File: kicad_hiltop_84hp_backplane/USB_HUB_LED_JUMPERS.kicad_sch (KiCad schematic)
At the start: 59 parts, among them U5 USB2517, Y2 24Mhz Xtal

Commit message: Added io tracking on the layout
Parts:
- R68, R69, R70, R71, R72, R73, R74, R75, R76, R77, R78, R79, R80, R81: value 330 -> 330R
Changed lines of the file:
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@@
     (in_bom yes) (on_board yes)
     (property "Reference" "R72" (id 0) (at 251.46 121.285 90))
-    (property "Value" "330" (id 1) (at 255.27 122.555 90))
+    (property "Value" "330R" (id 1) (at 255.27 122.555 90))
     (property "Footprint" "Resistor_SMD:R_0402_1005Metric" (id 2) (at 255.27 120.777 90)
       (effects (font (size 1.27 1.27)) hide)
@@
     (in_bom yes) (on_board yes)
     (property "Reference" "R73" (id 0) (at 251.46 125.095 90))
-    (property "Value" "330" (id 1) (at 255.27 126.365 90))
+    (property "Value" "330R" (id 1) (at 255.27 126.365 90))
     (property "Footprint" "Resistor_SMD:R_0402_1005Metric" (id 2) (at 255.27 124.587 90)
       (effects (font (size 1.27 1.27)) hide)
@@
     (in_bom yes) (on_board yes)
     (property "Reference" "R71" (id 0) (at 251.46 109.855 90))
-    (property "Value" "330" (id 1) (at 255.27 111.125 90))
+    (property "Value" "330R" (id 1) (at 255.27 111.125 90))
     (property "Footprint" "Resistor_SMD:R_0402_1005Metric" (id 2) (at 255.27 109.347 90)
       (effects (font (size 1.27 1.27)) hide)
@@
     (in_bom yes) (on_board yes)
     (property "Reference" "R70" (id 0) (at 251.46 106.045 90))
-    (property "Value" "330" (id 1) (at 255.27 107.315 90))
+    (property "Value" "330R" (id 1) (at 255.27 107.315 90))
     (property "Footprint" "Resistor_SMD:R_0402_1005Metric" (id 2) (at 255.27 105.537 90)
       (effects (font (size 1.27 1.27)) hide)
@@
     (in_bom yes) (on_board yes)
     (property "Reference" "R69" (id 0) (at 251.46 94.615 90))
-    (property "Value" "330" (id 1) (at 255.27 95.885 90))
+    (property "Value" "330R" (id 1) (at 255.27 95.885 90))
     (property "Footprint" "Resistor_SMD:R_0402_1005Metric" (id 2) (at 255.27 94.107 90)
       (effects (font (size 1.27 1.27)) hide)
@@
     (in_bom yes) (on_board yes)
     (property "Reference" "R68" (id 0) (at 251.46 90.805 90))
-    (property "Value" "330" (id 1) (at 255.27 92.075 90))
+    (property "Value" "330R" (id 1) (at 255.27 92.075 90))
     (property "Footprint" "Resistor_SMD:R_0402_1005Metric" (id 2) (at 255.27 90.297 90)
       (effects (font (size 1.27 1.27)) hide)
@@
     (in_bom yes) (on_board yes)
     (property "Reference" "R79" (id 0) (at 252.095 79.375 90))
-    (property "Value" "330" (id 1) (at 255.905 80.645 90))
+    (property "Value" "330R" (id 1) (at 255.905 80.645 90))
     (property "Footprint" "Resistor_SMD:R_0402_1005Metric" (id 2) (at 255.905 78.867 90)
       (effects (font (size 1.27 1.27)) hide)
@@
     (in_bom yes) (on_board yes)
     (property "Reference" "R78" (id 0) (at 252.095 75.565 90))
-    (property "Value" "330" (id 1) (at 255.905 76.835 90))
+    (property "Value" "330R" (id 1) (at 255.905 76.835 90))
     (property "Footprint" "Resistor_SMD:R_0402_1005Metric" (id 2) (at 255.905 75.057 90)
       (effects (font (size 1.27 1.27)) hide)
@@
     (in_bom yes) (on_board yes)
     (property "Reference" "R77" (id 0) (at 252.095 64.135 90))
-    (property "Value" "330" (id 1) (at 255.905 65.405 90))
+    (property "Value" "330R" (id 1) (at 255.905 65.405 90))
     (property "Footprint" "Resistor_SMD:R_0402_1005Metric" (id 2) (at 255.905 63.627 90)
       (effects (font (size 1.27 1.27)) hide)
@@
     (in_bom yes) (on_board yes)
     (property "Reference" "R76" (id 0) (at 252.095 60.325 90))
-    (property "Value" "330" (id 1) (at 255.905 61.595 90))
+    (property "Value" "330R" (id 1) (at 255.905 61.595 90))
     (property "Footprint" "Resistor_SMD:R_0402_1005Metric" (id 2) (at 255.905 59.817 90)
       (effects (font (size 1.27 1.27)) hide)
@@
     (in_bom yes) (on_board yes)
     (property "Reference" "R75" (id 0) (at 252.095 48.895 90))
-    (property "Value" "330" (id 1) (at 255.905 50.165 90))
+    (property "Value" "330R" (id 1) (at 255.905 50.165 90))
     (property "Footprint" "Resistor_SMD:R_0402_1005Metric" (id 2) (at 255.905 48.387 90)
       (effects (font (size 1.27 1.27)) hide)
@@
     (in_bom yes) (on_board yes)
     (property "Reference" "R74" (id 0) (at 252.095 45.085 90))
-    (property "Value" "330" (id 1) (at 255.905 46.355 90))
+    (property "Value" "330R" (id 1) (at 255.905 46.355 90))
     (property "Footprint" "Resistor_SMD:R_0402_1005Metric" (id 2) (at 255.905 44.577 90)
       (effects (font (size 1.27 1.27)) hide)
@@
     (in_bom yes) (on_board yes)
     (property "Reference" "R81" (id 0) (at 252.73 33.655 90))
-    (property "Value" "330" (id 1) (at 256.54 34.925 90))
+    (property "Value" "330R" (id 1) (at 256.54 34.925 90))
     (property "Footprint" "Resistor_SMD:R_0402_1005Metric" (id 2) (at 256.54 33.147 90)
       (effects (font (size 1.27 1.27)) hide)
@@
     (in_bom yes) (on_board yes)
     (property "Reference" "R80" (id 0) (at 252.73 29.845 90))
-    (property "Value" "330" (id 1) (at 256.54 31.115 90))
+    (property "Value" "330R" (id 1) (at 256.54 31.115 90))
     (property "Footprint" "Resistor_SMD:R_0402_1005Metric" (id 2) (at 256.54 29.337 90)
       (effects (font (size 1.27 1.27)) hide)

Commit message: finished tracking on board
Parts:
- R58, R59: footprint Resistor_SMD:R_0603_1608Metric -> Resistor_SMD:R_0402_1005Metric
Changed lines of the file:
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@@
     (property "Reference" "R59" (id 0) (at 137.795 54.61 90))
     (property "Value" "DNP" (id 1) (at 139.7 54.61 90))
-    (property "Footprint" "Resistor_SMD:R_0603_1608Metric" (id 2) (at 141.478 54.61 90)
+    (property "Footprint" "Resistor_SMD:R_0402_1005Metric" (id 2) (at 141.478 54.61 90)
       (effects (font (size 1.27 1.27)) hide)
     )
@@
     (property "Reference" "R58" (id 0) (at 137.795 34.29 90))
     (property "Value" "10K" (id 1) (at 139.7 34.29 90))
-    (property "Footprint" "Resistor_SMD:R_0603_1608Metric" (id 2) (at 141.478 34.29 90)
+    (property "Footprint" "Resistor_SMD:R_0402_1005Metric" (id 2) (at 141.478 34.29 90)
       (effects (font (size 1.27 1.27)) hide)
     )

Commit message: added stitching vias
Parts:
- C38, C43, C44, C45, C46, C47, C48, C50, C51, C52, C53, C54: footprint Capacitor_SMD:C_0603_1608Metric -> Capacitor_SMD:C_0402_1005Metric
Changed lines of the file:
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@@
       (effects (font (size 1.27 1.27)) (justify right))
     )
-    (property "Footprint" "Capacitor_SMD:C_0603_1608Metric" (id 2) (at 127.3048 115.57 0)
+    (property "Footprint" "Capacitor_SMD:C_0402_1005Metric" (id 2) (at 127.3048 115.57 0)
       (effects (font (size 1.27 1.27)) hide)
     )
@@
       (effects (font (size 1.27 1.27)) (justify right))
     )
-    (property "Footprint" "Capacitor_SMD:C_0603_1608Metric" (id 2) (at 134.9248 115.57 0)
+    (property "Footprint" "Capacitor_SMD:C_0402_1005Metric" (id 2) (at 134.9248 115.57 0)
       (effects (font (size 1.27 1.27)) hide)
     )
@@
       (effects (font (size 1.27 1.27)) (justify right))
     )
-    (property "Footprint" "Capacitor_SMD:C_0603_1608Metric" (id 2) (at 142.5448 115.57 0)
+    (property "Footprint" "Capacitor_SMD:C_0402_1005Metric" (id 2) (at 142.5448 115.57 0)
       (effects (font (size 1.27 1.27)) hide)
     )
@@
       (effects (font (size 1.27 1.27)) (justify right))
     )
-    (property "Footprint" "Capacitor_SMD:C_0603_1608Metric" (id 2) (at 150.1648 115.57 0)
+    (property "Footprint" "Capacitor_SMD:C_0402_1005Metric" (id 2) (at 150.1648 115.57 0)
       (effects (font (size 1.27 1.27)) hide)
     )
@@
       (effects (font (size 1.27 1.27)) (justify right))
     )
-    (property "Footprint" "Capacitor_SMD:C_0603_1608Metric" (id 2) (at 157.7848 115.57 0)
+    (property "Footprint" "Capacitor_SMD:C_0402_1005Metric" (id 2) (at 157.7848 115.57 0)
       (effects (font (size 1.27 1.27)) hide)
     )
@@
       (effects (font (size 1.27 1.27)) (justify right))
     )
-    (property "Footprint" "Capacitor_SMD:C_0603_1608Metric" (id 2) (at 165.4048 115.57 0)
+    (property "Footprint" "Capacitor_SMD:C_0402_1005Metric" (id 2) (at 165.4048 115.57 0)
       (effects (font (size 1.27 1.27)) hide)
     )
@@
       (effects (font (size 1.27 1.27)) (justify right))
     )
-    (property "Footprint" "Capacitor_SMD:C_0603_1608Metric" (id 2) (at 143.1798 101.6 0)
+    (property "Footprint" "Capacitor_SMD:C_0402_1005Metric" (id 2) (at 143.1798 101.6 0)
       (effects (font (size 1.27 1.27)) hide)
     )
@@
       (effects (font (size 1.27 1.27)) (justify right))
     )
-    (property "Footprint" "Capacitor_SMD:C_0603_1608Metric" (id 2) (at 127.9398 101.6 0)
+    (property "Footprint" "Capacitor_SMD:C_0402_1005Metric" (id 2) (at 127.9398 101.6 0)
       (effects (font (size 1.27 1.27)) hide)
     )
@@
       (effects (font (size 1.27 1.27)) (justify left))
     )
-    (property "Footprint" "Capacitor_SMD:C_0603_1608Metric" (id 2) (at 59.055 19.3548 0)
+    (property "Footprint" "Capacitor_SMD:C_0402_1005Metric" (id 2) (at 59.055 19.3548 0)
       (effects (font (size 1.27 1.27)) hide)
     )
@@
       (effects (font (size 1.27 1.27)) (justify left))
     )
-    (property "Footprint" "Capacitor_SMD:C_0603_1608Metric" (id 2) (at 41.6052 72.39 0)
+    (property "Footprint" "Capacitor_SMD:C_0402_1005Metric" (id 2) (at 41.6052 72.39 0)
       (effects (font (size 1.27 1.27)) hide)
     )
@@
       (effects (font (size 1.27 1.27)) (justify left))
     )
-    (property "Footprint" "Capacitor_SMD:C_0603_1608Metric" (id 2) (at 58.0898 100.33 0)
+    (property "Footprint" "Capacitor_SMD:C_0402_1005Metric" (id 2) (at 58.0898 100.33 0)
       (effects (font (size 1.27 1.27)) hide)
     )
@@
       (effects (font (size 1.27 1.27)) (justify left))
     )
-    (property "Footprint" "Capacitor_SMD:C_0603_1608Metric" (id 2) (at 58.0898 111.76 0)
-      (effects (font (size 1.27 1.27)) hide)
-    )
+    (property "Footprint" "Capacitor_SMD:C_0402_1005Metric" (id 2) (at 58.0898 111.76 0)
+      (effects (font (size 1.27 1.27)) hide)
+    )

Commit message: Layout finished and gerbers exported
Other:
- title: 63HP HILTOP Backplane -> 84HP HILTOP Backplane
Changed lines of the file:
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@@
   (paper "A4")
   (title_block
-    (title "63HP HILTOP Backplane")
-    (date "2021-02-04")
-    (rev "C")
+    (title "84HP HILTOP Backplane")
+    (date "2023-04-06")
+    (rev "A")
     (company "Devtank Ltd")
+    (comment 1 "Part No: 304-020")
   )
   (junction (at 59.055 110.49) (diameter 0) (color 0 0 0 0)

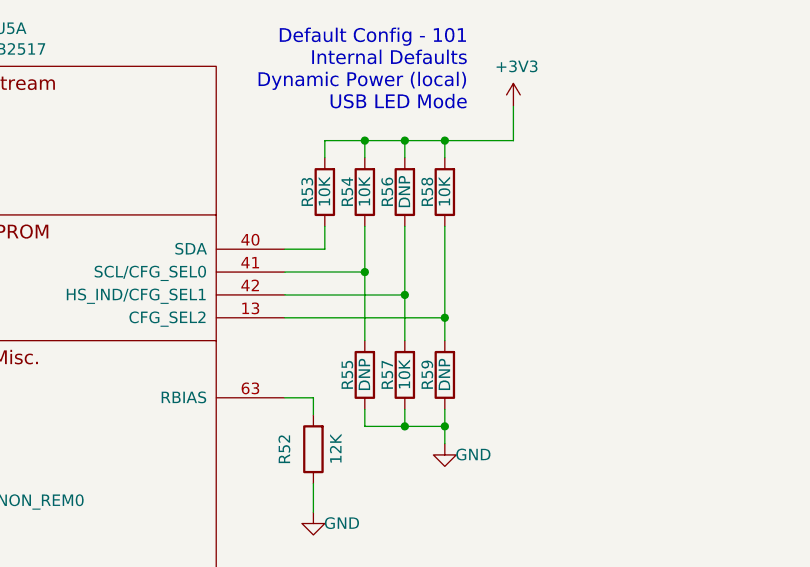
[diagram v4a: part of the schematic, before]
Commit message: added measurments to layout
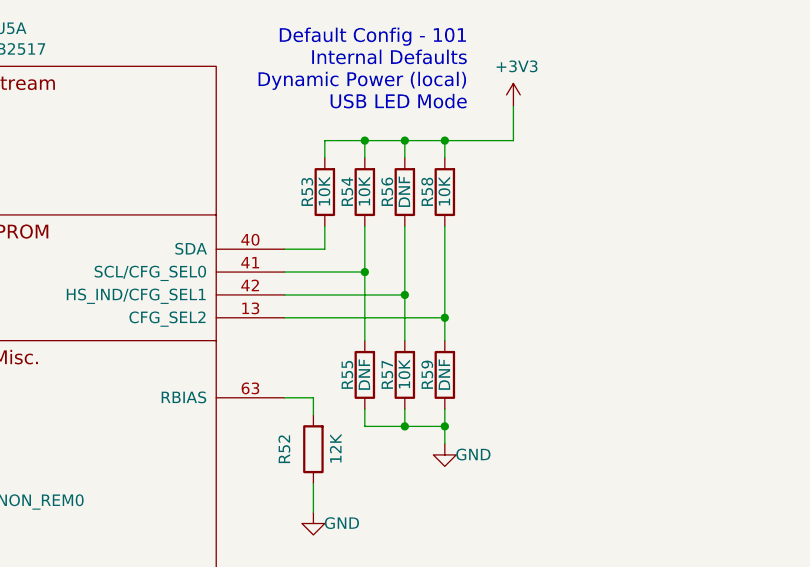
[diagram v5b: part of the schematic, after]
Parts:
- C38, C39, C40, C41, C42, C43, C44, C45, C46, C47, C48, C49, C50, C51, C52, C53, C54: Characteristics (none) -> X5R; Voltage (none) -> 10V
- D14, D16, D18, D20, D22, D24, D26: Manufacturer (none) -> Rohm Semiconductor; Manufacturer Part Number (none) -> SML-P13PTT86R
- D15, D17, D19, D21, D23, D25, D27: Manufacturer (none) -> Rohm Semiconductor; Manufacturer Part Number (none) -> SML-P11MTT86R
- R48, R49, R50, R51, R52, R53, R54, R57, R58, R68, R69, R70, R71, R72, R73, R74, R75, R76, R77, R78, R79, R80, R81: Tolerance (none) -> 1%
- R55, R56, R59: value DNP -> DNF; Tolerance (none) -> 1%
- U5: Manufacturer (none) -> Microchip; Manufacturer Part Number (none) -> USB2517-JZX
- Y2: Manufacturer (none) -> AEL Crystals; Manufacturer Part Number (none) -> X24M000000S050
